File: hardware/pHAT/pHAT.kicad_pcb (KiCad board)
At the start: 2 copper layers, 65 x 30 mm, 24 parts, among them P1 Conn_02x20_Odd_Even, U1 ADC101C021CIMK, U2 P82B96, U3 P82B96

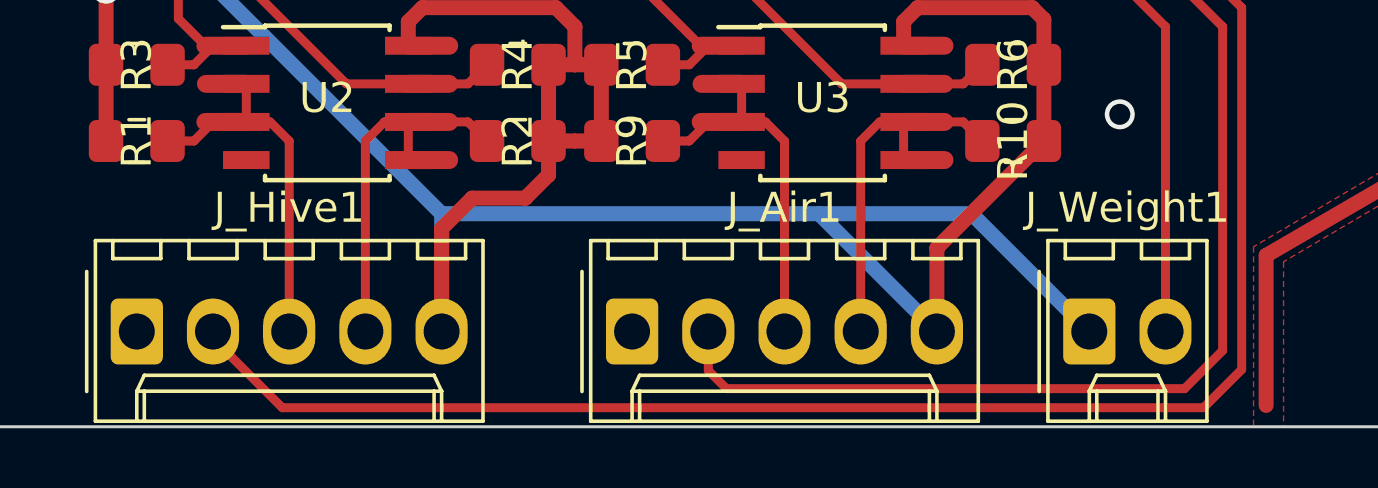
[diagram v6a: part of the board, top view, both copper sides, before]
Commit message: Adding smd pad for connectors
Adding SMD pads to allow surface soldering at right angle of Molex JYK connectors
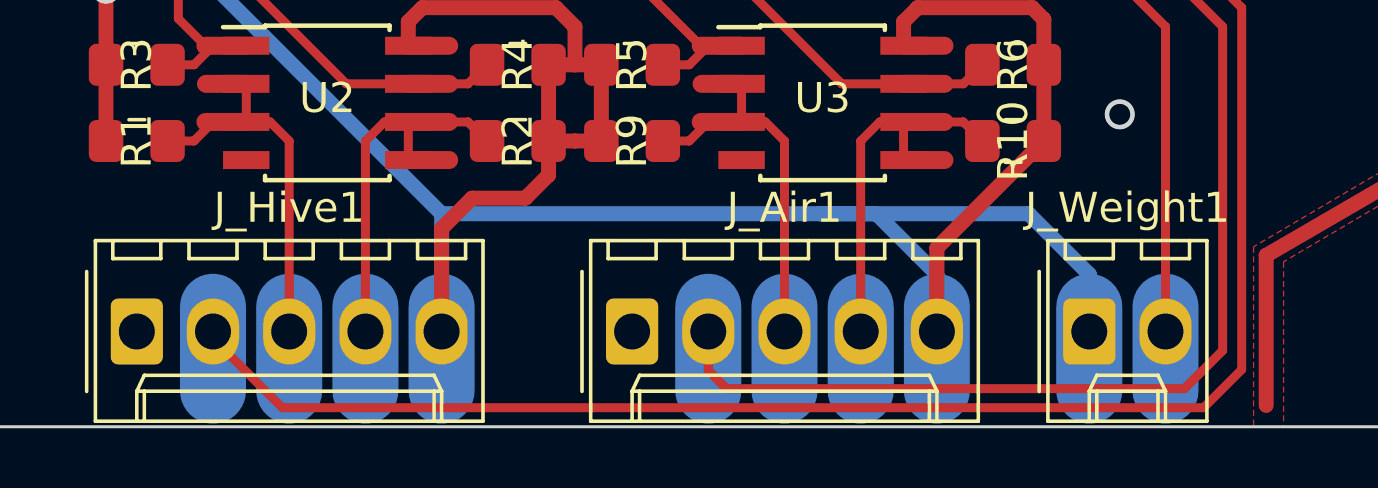
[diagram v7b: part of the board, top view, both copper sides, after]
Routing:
- net +3V3: track 187.1 -> 197.2 mm
- net /SDAA: track 14.9 -> 17.7 mm
- net /SCLA: track 14.9 -> 17.7 mm
- net /alarm_air: track 46.9 -> 49.7 mm
- net /SDAH: track 14.9 -> 17.7 mm
- net /SCLH: track 14.9 -> 17.7 mm
- net /AnalogIn: track 32.5 -> 35.3 mm
- net /alarm_hive: track 63.5 -> 66.3 mm
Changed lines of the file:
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@@
     (thickness 1.6)
     (drawings 15)
-    (tracks 169)
+    (tracks 180)
     (zones 0)
     (modules 24)
@@
   (gr_line (start 265 147) (end 265 123) (layer Edge.Cuts) (width 0.1))
   (gr_line (start 203 150) (end 262 150) (layer Edge.Cuts) (width 0.1))
+  (segment (start 243.815 146) (end 243.815 148.8) (width 2.2) (layer B.Cu) (net 31))
+  (segment (start 241.275 146) (end 241.275 148.8) (width 2.2) (layer B.Cu) (net 1))
+  (segment (start 236.195 146) (end 236.195 148.8) (width 2.2) (layer B.Cu) (net 1))
+  (segment (start 233.655 146) (end 233.655 148.8) (width 2.2) (layer B.Cu) (net 35))
+  (segment (start 231.115 146) (end 231.115 148.8) (width 2.2) (layer B.Cu) (net 36))
+  (segment (start 228.575 146) (end 228.575 148.8) (width 2.2) (layer B.Cu) (net 38))
+  (segment (start 212.065 146) (end 212.065 148.8) (width 2.2) (layer B.Cu) (net 37))
+  (segment (start 214.605 146) (end 214.605 148.8) (width 2.2) (layer B.Cu) (net 33))
+  (segment (start 217.145 146) (end 217.145 148.8) (width 2.2) (layer B.Cu) (net 34))
   (segment (start 235.085 137.3) (end 236.449 137.3) (width 0.6) (layer F.Cu) (net 1))
   (segment (start 229.878 129.619) (end 228.489 129.619) (width 0.65) (layer F.Cu) (net 1))
@@
   (segment (start 209.136396 135.395) (end 208.5 135.395) (width 0.5) (layer B.Cu) (net 1))
   (segment (start 219.685 142.9) (end 212.18 135.395) (width 0.5) (layer B.Cu) (net 1))
-  (segment (start 236.16 146.79) (end 232.27 142.9) (width 0.5) (layer B.Cu) (net 1))
-  (segment (start 236.195 146.56) (end 236.195 146.79) (width 0.5) (layer B.Cu) (net 1))
-  (segment (start 236.195 146.79) (end 236.16 146.79) (width 0.5) (layer B.Cu) (net 1))
-  (segment (start 237.35 142.9) (end 232.27 142.9) (width 0.5) (layer B.Cu) (net 1))
-  (segment (start 241.275 146.825) (end 237.35 142.9) (width 0.5) (layer B.Cu) (net 1))
   (segment (start 232.27 142.9) (end 219.685 142.9) (width 0.5) (layer B.Cu) (net 1))
   (segment (start 236.195 144.04) (end 239.76 140.475) (width 0.5) (layer F.Cu) (net 1))
@@
   (segment (start 219.045 136.03) (end 218.575 136.5) (width 0.5) (layer F.Cu) (net 1))
   (segment (start 232.469 129.544) (end 230.564 129.544) (width 0.5) (layer F.Cu) (net 1))
+  (segment (start 219.685 146) (end 219.685 148.8) (width 2.2) (layer B.Cu) (net 1))
+  (segment (start 234.175 142.9) (end 232.27 142.9) (width 0.5) (layer B.Cu) (net 1))
+  (segment (start 236.195 146.56) (end 236.195 144.92) (width 0.5) (layer B.Cu) (net 1))
+  (segment (start 236.195 144.92) (end 234.175 142.9) (width 0.5) (layer B.Cu) (net 1))
+  (segment (start 239.255 142.9) (end 232.27 142.9) (width 0.5) (layer B.Cu) (net 1))
+  (segment (start 241.275 146.825) (end 241.275 144.92) (width 0.5) (layer B.Cu) (net 1))
+  (segment (start 241.275 144.92) (end 239.255 142.9) (width 0.5) (layer B.Cu) (net 1))
   (segment (start 229.5 130.569) (end 228.489 130.569) (width 0.65) (layer F.Cu) (net 2))
   (segment (start 234.374 131.594) (end 230.564 131.594) (width 0.5) (layer F.Cu) (net 2))

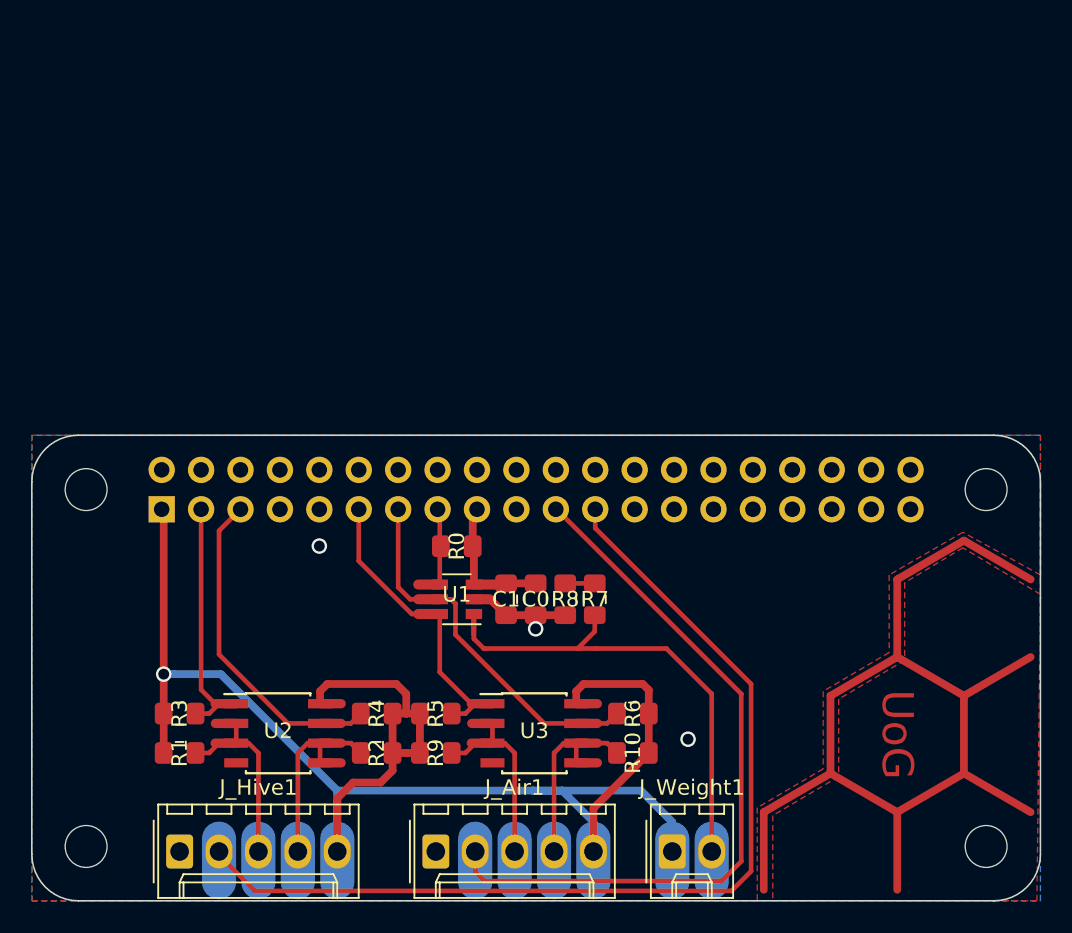
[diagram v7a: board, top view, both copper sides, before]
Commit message: Sensor Board v3.0
Removed ADC converter, moved the hive temp&hum sensor to the main board that will now be placed inside the hive
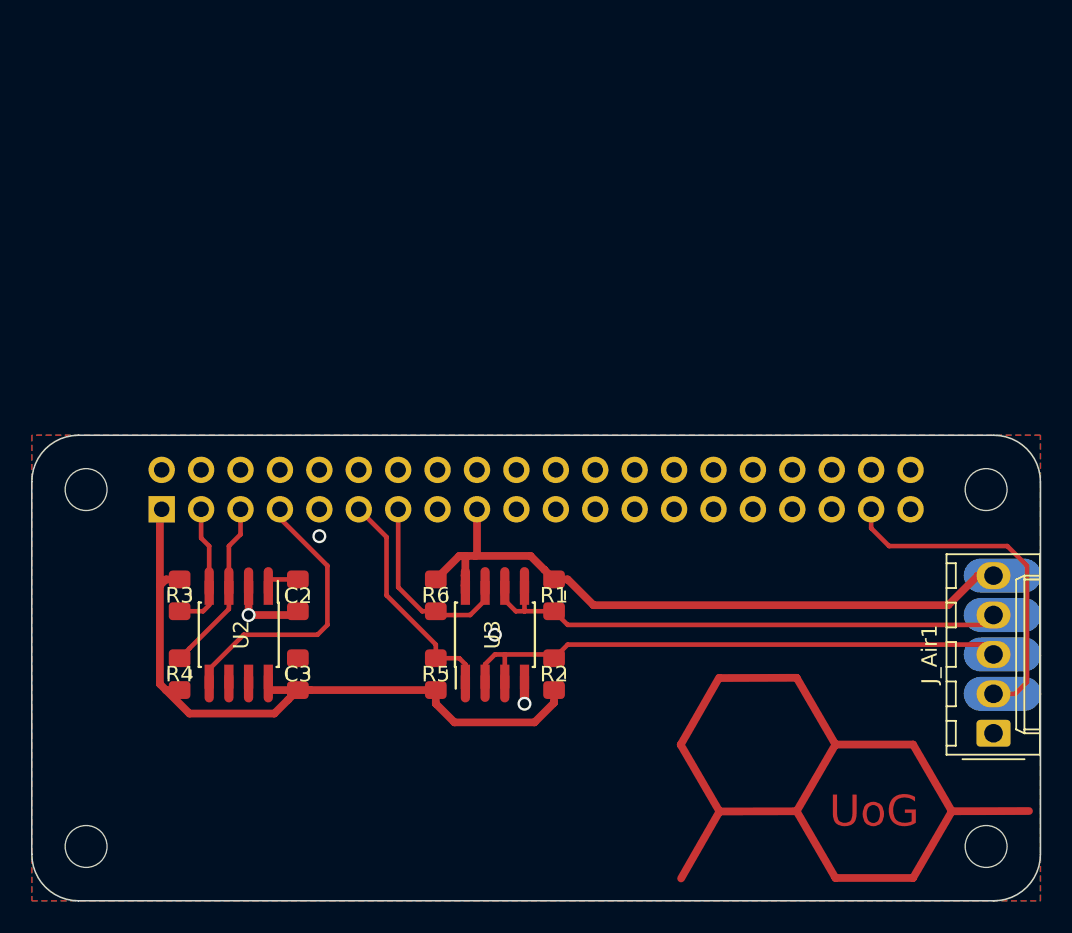
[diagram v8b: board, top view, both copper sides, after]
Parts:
- removed C0: 0.1µ, Capacitor_SMD:C_0805_2012Metric_Pad1.15x1.40mm_HandSolder
- removed C1: 4.7µ, Capacitor_SMD:C_0805_2012Metric_Pad1.15x1.40mm_HandSolder
- removed J_Hive1: Conn_01x05, Connector_Molex:Molex_KK-254_AE-6410-05A_1x05_P2.54mm_Vertical
- removed J_Weight1: Conn_01x02, Connector_Molex:Molex_KK-254_AE-6410-02A_1x02_P2.54mm_Vertical
- removed R0, R10, R7, R8, R9: 5K, Resistor_SMD:R_0805_2012Metric_Pad1.15x1.40mm_HandSolder
- removed U1: ADC101C021CIMK, Package_TO_SOT_SMD:SOT-23-6
- added C2: 0.1µ, Capacitor_SMD:C_0805_2012Metric_Pad1.15x1.40mm_HandSolder, F.Cu at (217.1, 130.3)
- added C3: 0.22µ, Capacitor_SMD:C_0805_2012Metric_Pad1.15x1.40mm_HandSolder, F.Cu at (217.1, 135.4)
- U2: value P82B96 -> HIH6131-021
- moved J_Air1 36.7 mm to (262.0, 139.2), turned to 90 degrees
- moved R1 26.2 mm to (233.7, 130.3), turned to 270 degrees
- moved R6 14.8 mm to (226.0, 130.3), turned to 270 degrees
- moved R4 13.0 mm to (209.5, 135.4), turned to 90 degrees
- moved R2 12.5 mm to (233.7, 135.4), turned to 90 degrees
- moved R3 7.62 mm to (209.5, 130.3), turned to 270 degrees
- moved U2 6.84 mm to (213.3, 132.9), turned to 270 degrees
- moved U3 6.84 mm to (229.8, 132.9), turned to 90 degrees
- moved R5 2.54 mm to (226.0, 135.4), turned to 90 degrees
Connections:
- P1 pad 15: /ADC_Alert -> Net-(P1-Pad15)
- P1 pad 21: /alarm_air -> Net-(P1-Pad21)
- P1 pad 23: /alarm_hive -> Net-(P1-Pad23)
- P1 pad 37: Net-(P1-Pad37) -> /alarm_air
- P1 pad 7: Net-(P1-Pad7) -> /alarm_hive
- R1 pad 2: /SDAH -> /SCLA
- R2 pad 2: /SCLH -> /SDAA
- U2 pad 1: /SDA0 -> /Vcore
- U2 pad 2: /SDAH -> GND
- U2 pad 3: /SDAH -> /SCL0
- U2 pad 4: GND -> /SDA0
- U2 pad 5: /SCLH -> /alarm_hive
- U2 pad 6: /SCLH -> Net-(U2-Pad6)
- U2 pad 7: /SCL0 -> Net-(U2-Pad7)
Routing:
- net +3V3: track 197.2 -> 96.1 mm, vias 1 -> 0
- net (no net): track 0.00 -> 64.7 mm
- net /alarm_hive: track 66.3 -> 19.4 mm
- net /AnalogIn: track 35.3 -> 0.00 mm
- net /SDAA: track 17.7 -> 42.6 mm
- net /alarm_air: track 49.7 -> 25.0 mm
- net /SCLA: track 17.7 -> 39.6 mm
- net /SCLH: track 17.7 -> 0.00 mm
- net /SDAH: track 17.7 -> 0.00 mm
- net /SCL1: track 26.0 -> 13.6 mm
- net /SCL0: track 22.5 -> 11.2 mm
- net /SDA0: track 17.4 -> 8.46 mm
- net /ADC_Alert: track 6.70 -> 0.00 mm
- net /Vcore: track 0.00 -> 4.36 mm
- net /SDA1: track 19.5 -> 15.9 mm
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- removed copper zone on F.Cu, net (none)
